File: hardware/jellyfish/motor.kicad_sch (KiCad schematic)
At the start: 24 parts, among them J7 MOTOR, U8 TMC2209

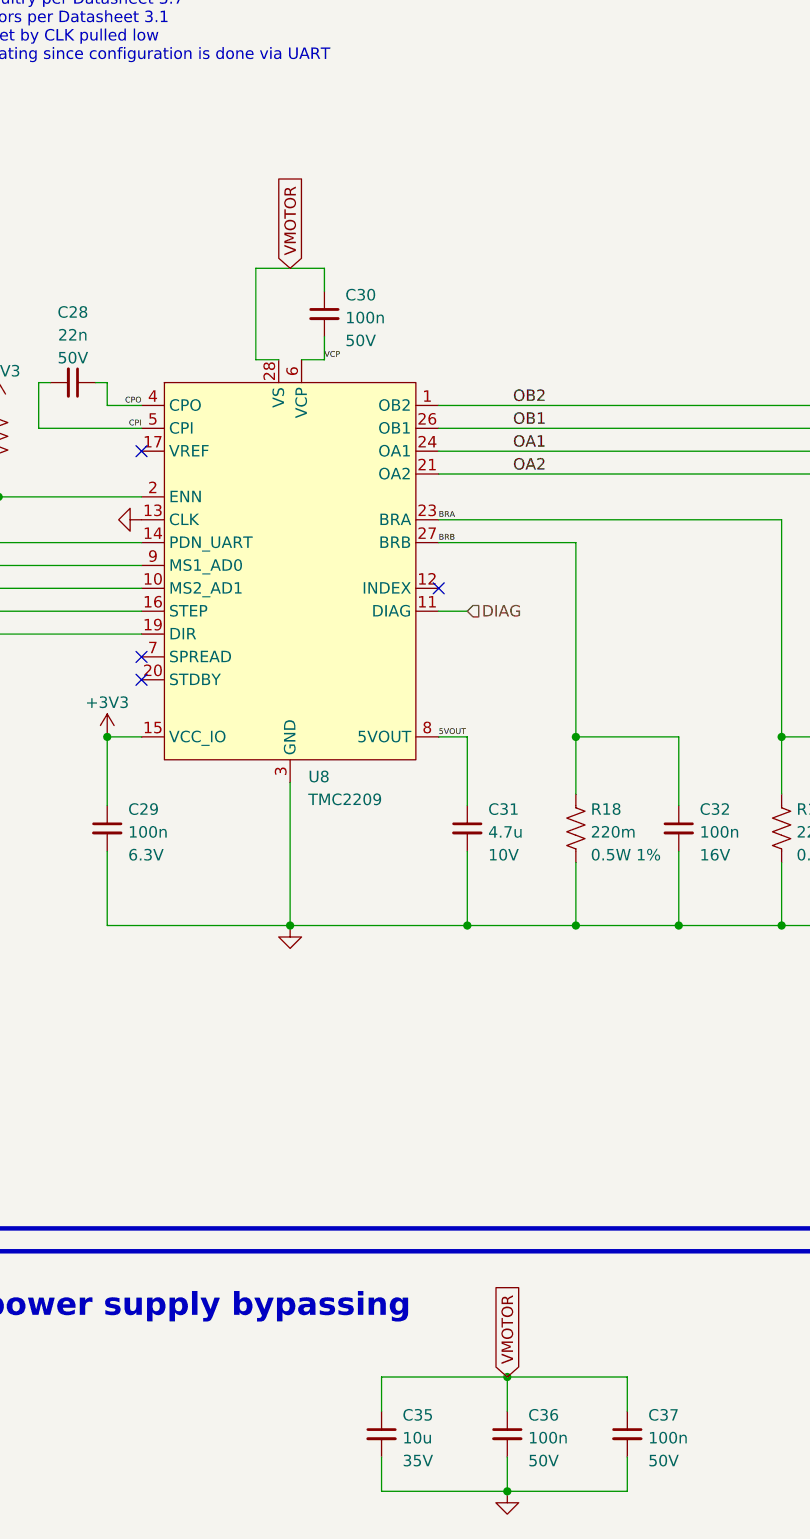
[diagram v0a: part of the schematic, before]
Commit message: Update Jellyfish with some stuff from Starfish
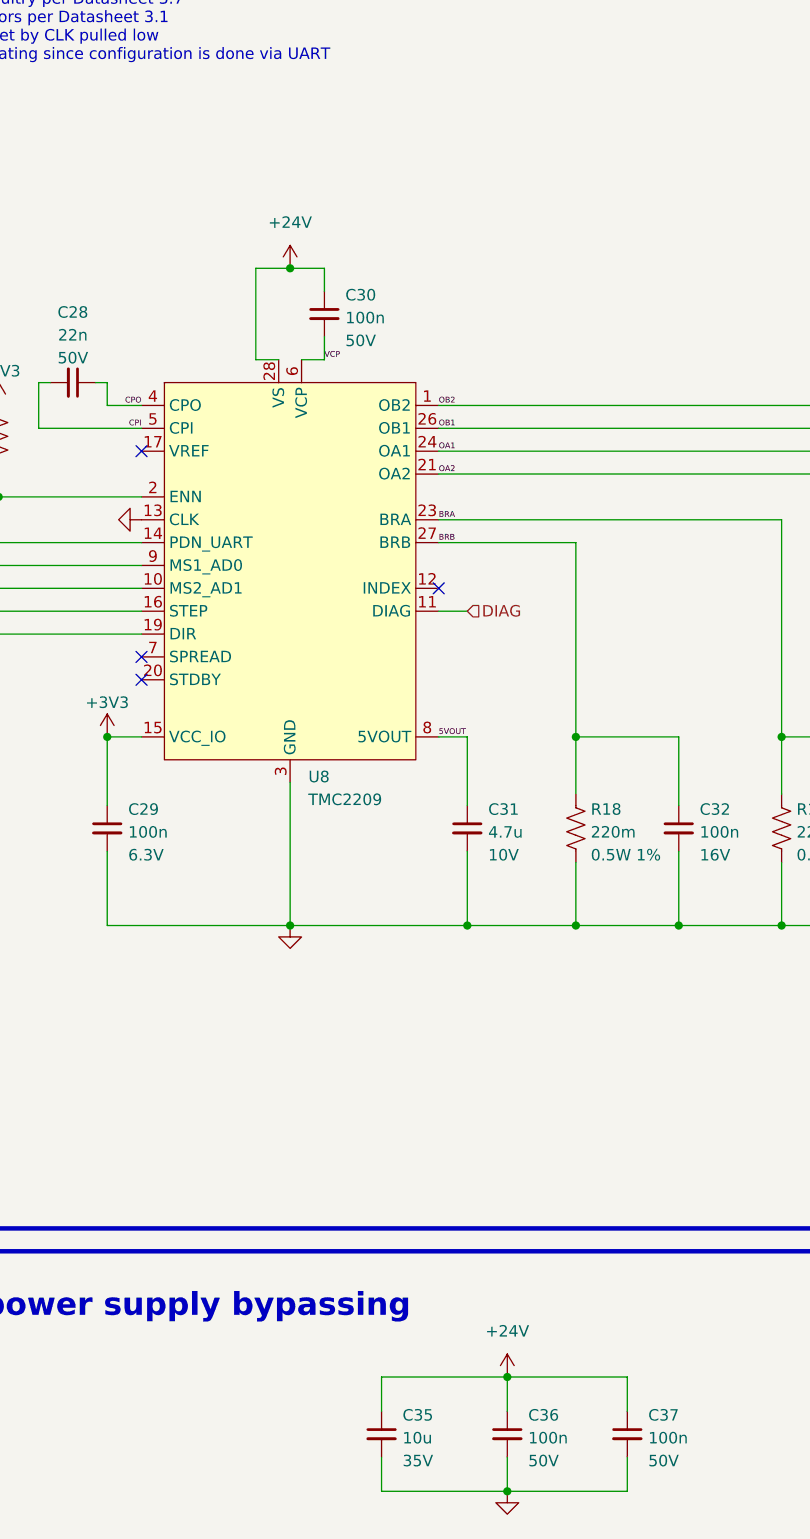
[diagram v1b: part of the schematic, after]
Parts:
- C28, C30, C31, C36, C37, C38, C39, C40, C41: footprint Capacitor_SMD:C_0603_1608Metric_Pad1.08x0.95mm_HandSolder -> winterbloom:C_0603_HandSolder
- C29, C32, C33: footprint Capacitor_SMD:C_0402_1005Metric_Pad0.74x0.62mm_HandSolder -> winterbloom:C_0402_HandSolder
- C35: footprint Capacitor_SMD:C_1210_3225Metric_Pad1.33x2.70mm_HandSolder -> winterbloom:C_1210_HandSolder
- FB2, FB3, FB4, FB5: footprint Inductor_SMD:L_0603_1608Metric_Pad1.05x0.95mm_HandSolder -> winterbloom:L_0603_HandSolder
- J7: footprint Connector_JST:JST_XH_B4B-XH-AM_1x04_P2.50mm_Vertical -> winterbloom:JST_XH_B4B-XH-AM_1x04_P2.50mm_Vertical
- R17: footprint Resistor_SMD:R_0402_1005Metric_Pad0.72x0.64mm_HandSolder -> winterbloom:R_0402_HandSolder
- R18, R19: footprint Resistor_SMD:R_1206_3216Metric_Pad1.30x1.75mm_HandSolder -> winterbloom:R_1206_HandSolder
- RV2, RV3: footprint Resistor_SMD:R_0603_1608Metric_Pad0.98x0.95mm_HandSolder -> winterbloom:R_0603_HandSolder
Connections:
- net VS renamed +24V
